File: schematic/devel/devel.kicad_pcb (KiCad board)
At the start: 4 copper layers, 63 x 40 mm, 45 parts, among them J1 CONN_PWR, J2 CONN_X1, J3 CONN_Y2, J4 CONN_X2, J5 CONN_Y1, U1 LM317_SOT223, U2 LM337_SOT223, U3 REF5010IDGK, U4 OPA4197

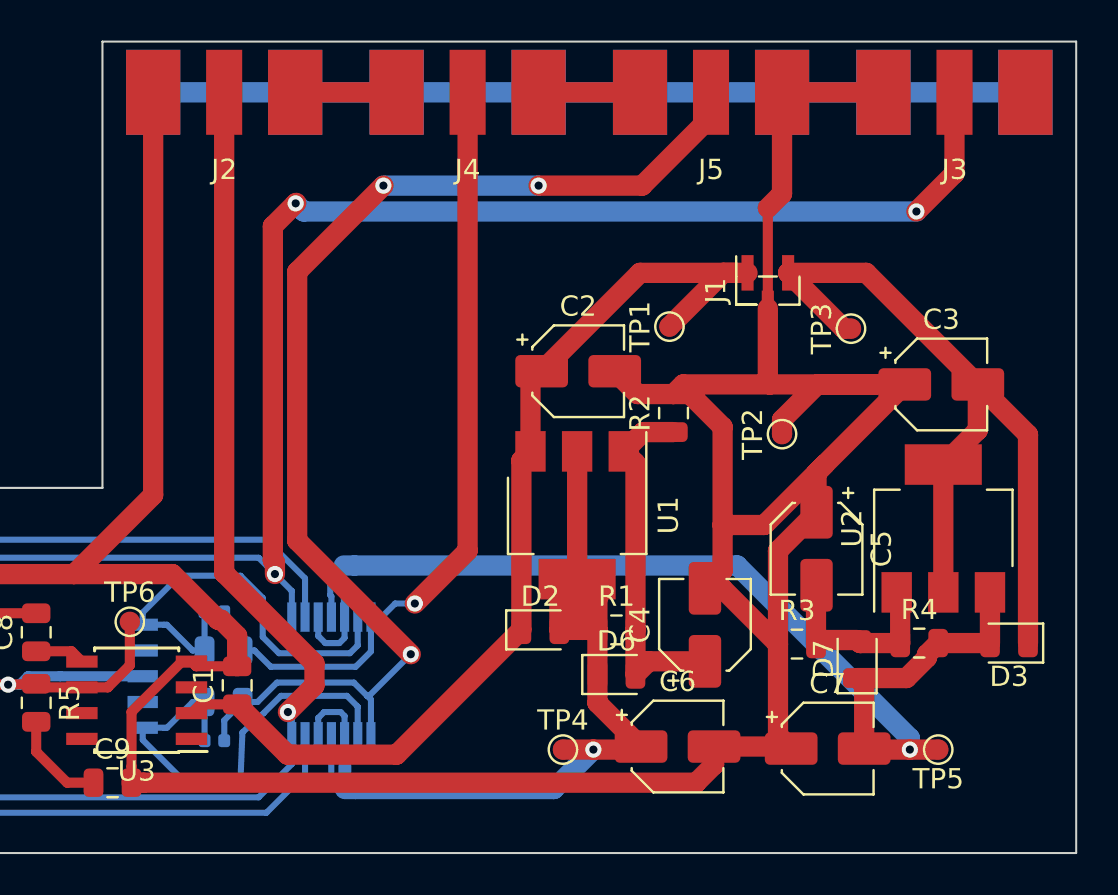
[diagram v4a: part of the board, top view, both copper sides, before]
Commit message: replaced sma connector footprint
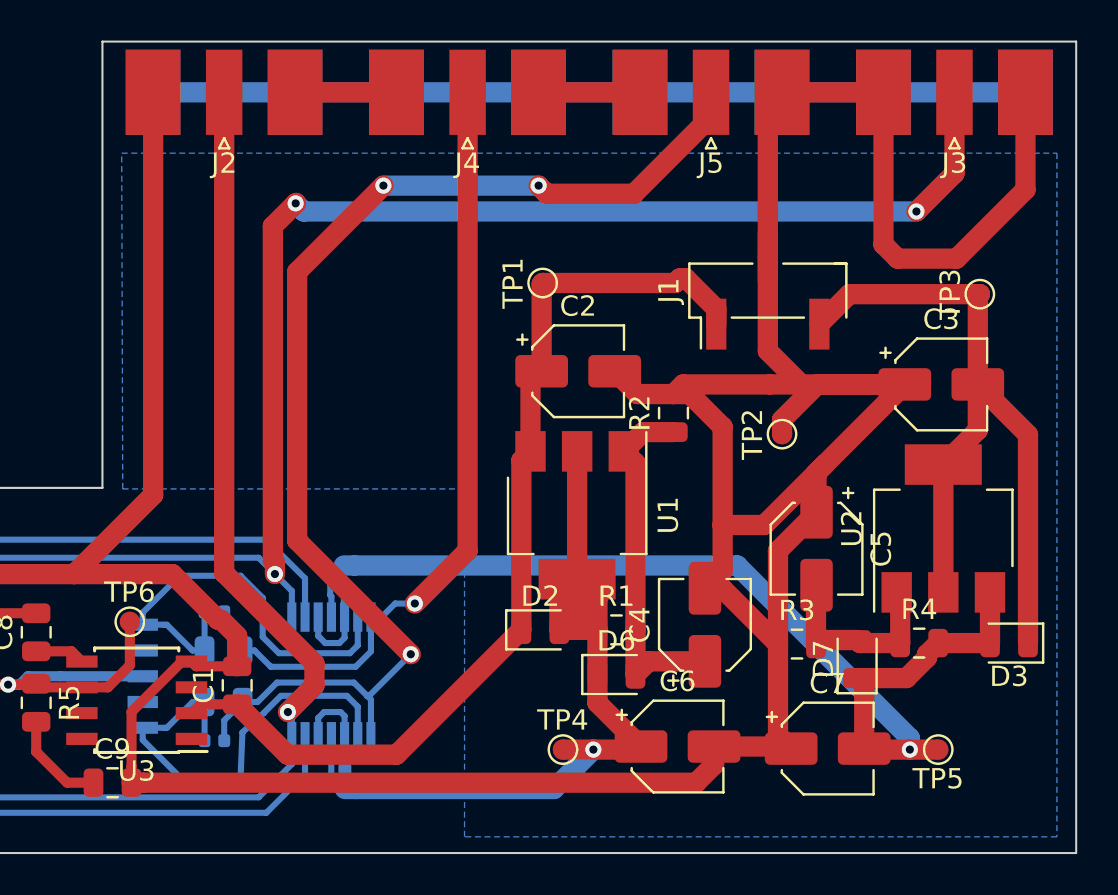
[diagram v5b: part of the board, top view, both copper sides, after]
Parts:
- J1: footprint Connector_PinHeader_1.00mm:PinHeader_1x03_P1.00mm_Vertical_SMD_Pin1Right -> Connector_PinHeader_2.54mm:PinHeader_1x03_P2.54mm_Vertical_SMD_Pin1Left
- J2, J3, J4, J5: footprint Connector_Coaxial_SMA:SMA_EdgeSlim -> Connector_Coaxial_SMA:SMA_Molex_73251-2120_EdgeMount
- moved TP1 6.61 mm to (121.7, 111.9)
- moved TP3 6.57 mm to (143.2, 112.5)
- turned J2 to 90 degrees
- turned J3 to 90 degrees
- turned J4 to 90 degrees
- turned J5 to 90 degrees
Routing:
- net GND: track 238.7 -> 260.3 mm
- net -15V: track 40.6 -> 37.7 mm
- net +15V: track 49.7 -> 47.6 mm
- added copper zone on In1.Cu, net (none)
- added copper zone on B.Cu, net GND
- added copper zone on In1.Cu, net GND
- added copper zone on In2.Cu, net GND

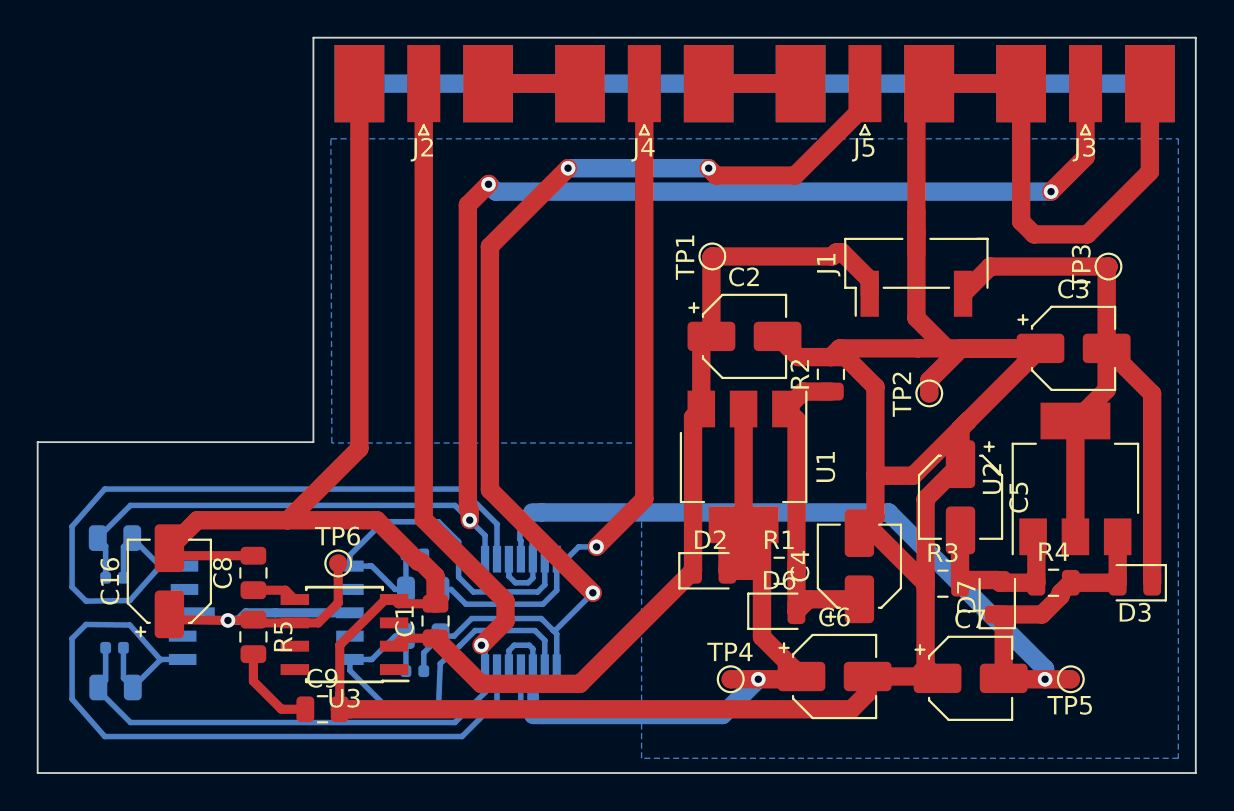
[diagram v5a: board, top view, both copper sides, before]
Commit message: completed pcb layout with cooper fills
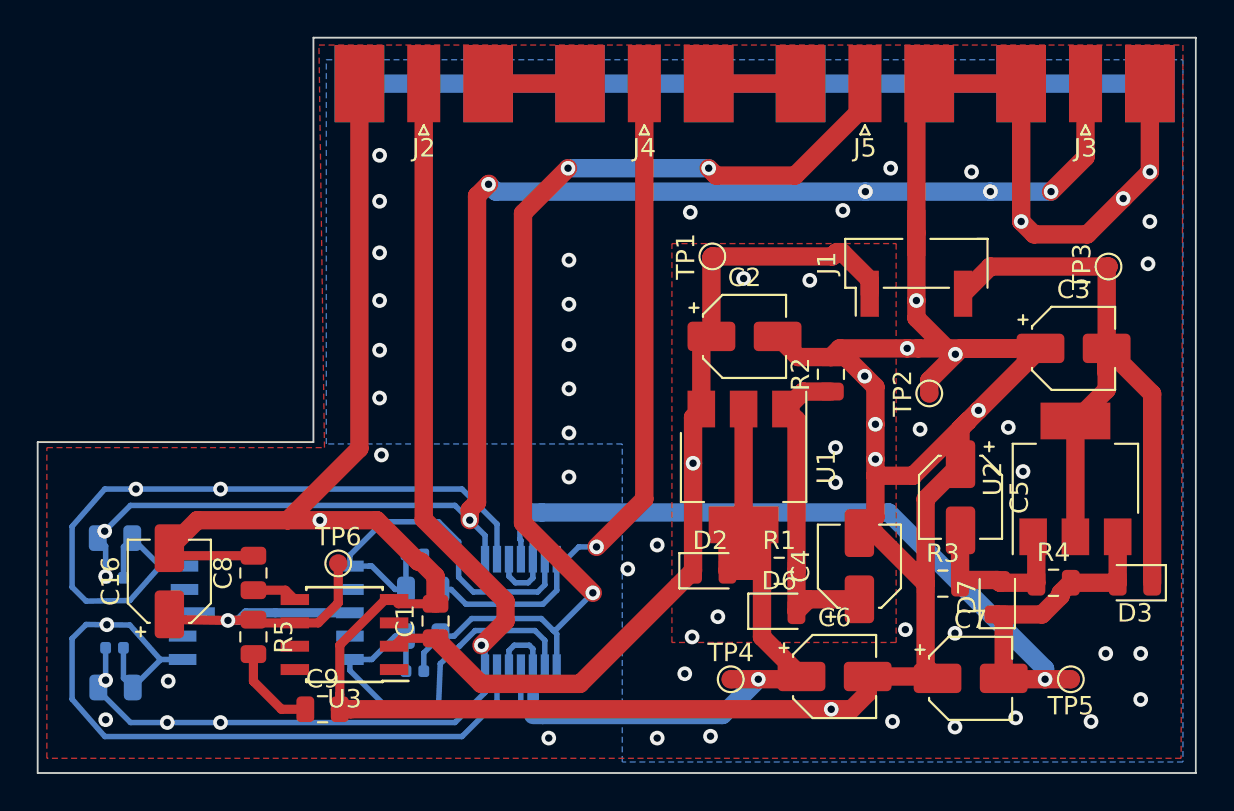
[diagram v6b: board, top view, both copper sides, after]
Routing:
- net Net-(C15-Pad2): track 60.5 -> 59.0 mm
- net -15V: track 37.7 -> 39.1 mm
- net Net-(C13-Pad2): vias 3 -> 7
- net Net-(C12-Pad1): vias 0 -> 1
- net Net-(C13-Pad1): vias 0 -> 2
- net Net-(C12-Pad2): vias 1 -> 4
- net GND: vias 0 -> 53
- net +15V: vias 0 -> 5
- added copper zone on F.Cu, net +15V
- added copper zone on F.Cu, net GND

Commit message: updated pcb layout, added screws
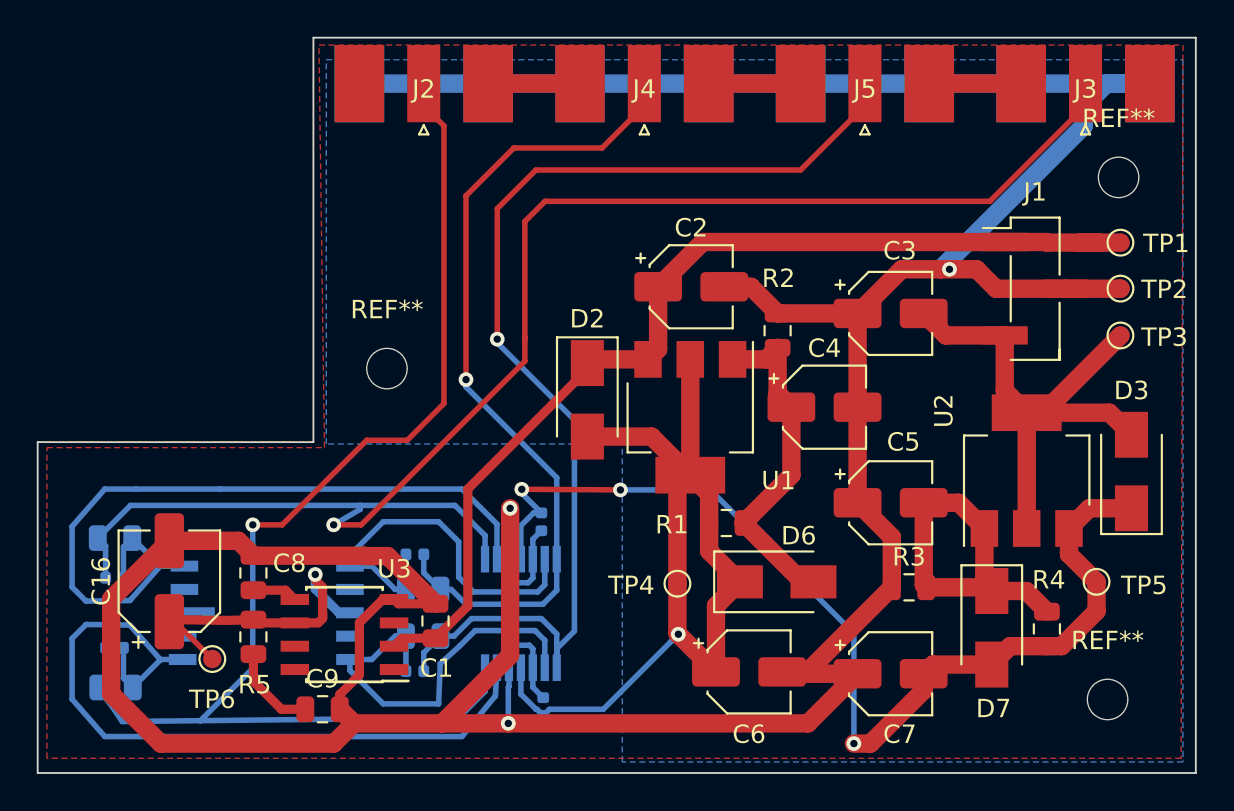
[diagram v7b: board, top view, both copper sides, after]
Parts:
- added ?: , , F.Cu at (143.3, 135.6)
- added ?: , , F.Cu at (143.9, 135.7)
- added ?: , , F.Cu at (105.7, 110.4)
- added REF**: MountingHole_2.2mm_M2, MountingHole:MountingHole_2.2mm_M2, F.Cu at (104.0, 118.0)
- added REF**: MountingHole_2.2mm_M2, MountingHole:MountingHole_2.2mm_M2, F.Cu at (143.8, 107.6)
- added REF**: MountingHole_2.2mm_M2, MountingHole:MountingHole_2.2mm_M2, F.Cu at (143.2, 136.0)
- C16: footprint Capacitor_SMD:CP_Elec_4x3.9 -> Capacitor_SMD:CP_Elec_5x5.3
- C2, C3: footprint Capacitor_SMD:CP_Elec_4x3.9 -> Capacitor_SMD:CP_Elec_4x5.4
- D2, D3, D6, D7: value 1N4001 -> S1A; footprint Diode_SMD:D_0805_2012Metric -> Diode_SMD:D_SMA
- R2, R3: value 980 -> 1k
- moved TP1 22.2 mm to (143.9, 111.2)
- moved TP2 11.9 mm to (143.9, 113.7)
- moved D2 11.5 mm to (114.9, 119.7), turned to 270 degrees
- moved C3 10.1 mm to (131.4, 115.0)
- moved C4 8.86 mm to (127.8, 120.1), turned to 0 degrees
- moved TP6 8.60 mm to (94.5, 133.8)
- moved J1 6.61 mm to (139.3, 113.7), turned to 0 degrees
- moved D3 6.05 mm to (144.5, 123.6), turned to 90 degrees
- moved TP4 5.95 mm to (119.8, 129.7)
- moved TP5 5.48 mm to (142.6, 129.6)
- moved C6 4.66 mm to (123.7, 134.5)
- moved C7 4.36 mm to (131.4, 134.6)
- moved C2 3.96 mm to (120.5, 113.5)
- moved U1 3.96 mm to (120.5, 120.7)
- moved R1 3.88 mm to (122.5, 126.4)
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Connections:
- D3 pad 1: -15V -> -12V
- D3 pad 2: -12V -> -15V
- D7 pad 1: -12V -> Net-(C5-Pad2)
- D7 pad 2: Net-(C5-Pad2) -> -12V
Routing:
- net GND: track 260.3 -> 235.3 mm, vias 53 -> 3
- net -15V: track 39.1 -> 28.9 mm
- net Net-(C5-Pad2): track 9.78 -> 19.2 mm
- net Net-(C12-Pad2): track 60.3 -> 69.0 mm, vias 4 -> 1
- net +15V: track 47.6 -> 55.7 mm, vias 5 -> 0
- net Net-(C14-Pad2): track 39.7 -> 45.9 mm
- net +12V: track 43.2 -> 49.3 mm
- net -12V: track 52.2 -> 58.0 mm, vias 1 -> 3
- net Net-(C15-Pad2): track 59.0 -> 61.8 mm, vias 3 -> 1
- net Net-(C13-Pad2): track 82.3 -> 84.1 mm, vias 7 -> 1
- net Net-(C16-Pad1): track 18.8 -> 17.6 mm
- net Net-(C4-Pad1): track 17.8 -> 18.7 mm
- net Net-(C12-Pad1): track 41.7 -> 41.6 mm, vias 1 -> 0
- net Net-(C13-Pad1): vias 2 -> 0
- removed copper zone on F.Cu, net +15V

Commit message: improved cooper fill zones
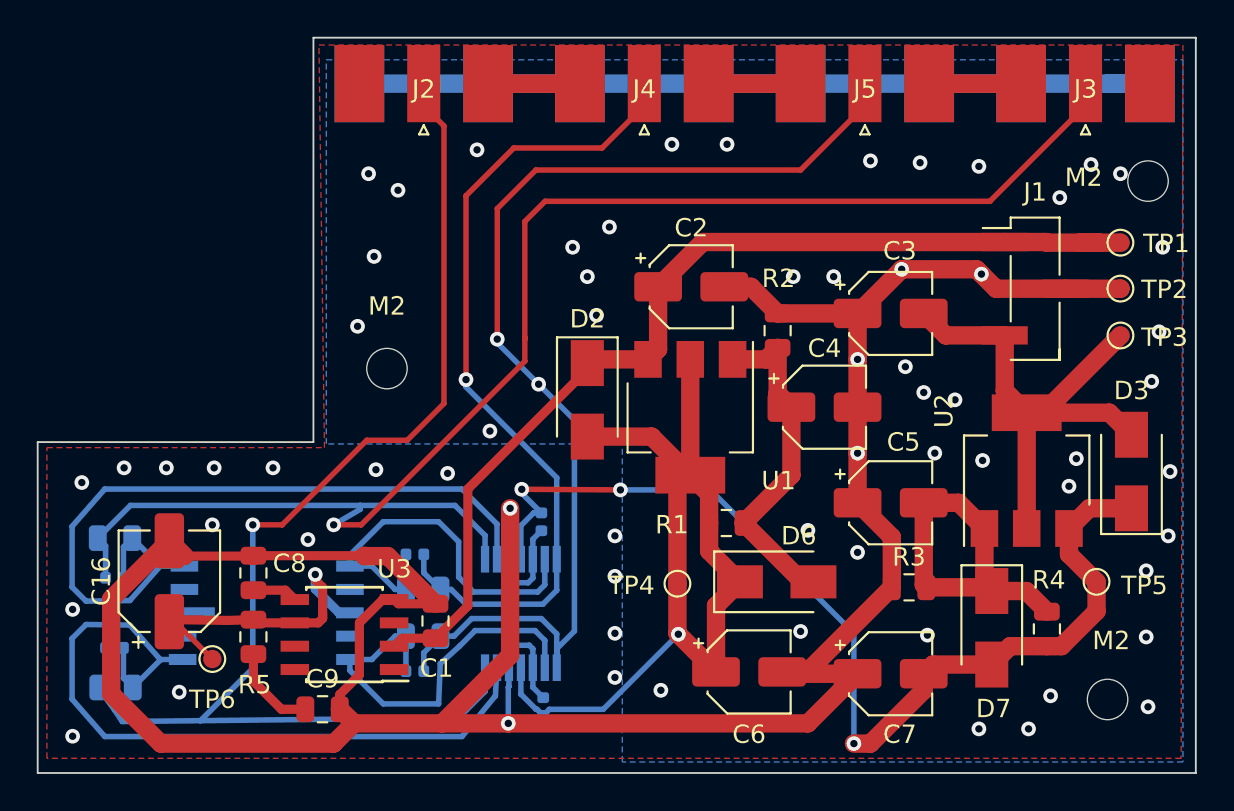
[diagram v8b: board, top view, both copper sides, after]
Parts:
- removed REF** (x2): MountingHole_2.2mm_M2, MountingHole:MountingHole_2.2mm_M2
- added M2: MountingHole_2.2mm_M2, MountingHole:MountingHole_2.2mm_M2, F.Cu at (145.4, 107.8)
- added M2: MountingHole_2.2mm_M2, MountingHole:MountingHole_2.2mm_M2, F.Cu at (143.2, 136.0)
- renumbered REF** to M2
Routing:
- net GND: track 235.3 -> 221.4 mm, vias 3 -> 64
- net Net-(C15-Pad2): vias 1 -> 2
- net (no net): vias 0 -> 1
